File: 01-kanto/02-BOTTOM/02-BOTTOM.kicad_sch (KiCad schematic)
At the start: 0 parts

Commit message: 基板は2枚だけさ
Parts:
- added C2, C3, C4, C5, C6, C7, C9: 100n, symbol Device:C
- added C8: 4.7u, symbol Device:C
- added D2, D3, D4, D5: WS2812B, LED_SMD:LED_WS2812B_PLCC4_5.0x5.0mm_P3.2mm, symbol LED:WS2812B
- added R11, R12, R13, R14: 10k, symbol Device:R
- added SW6, SW7: SW_Push, symbol Switch:SW_Push
- added U2: STM32F103C8Tx, Package_QFP:LQFP-48_7x7mm_P0.5mm, symbol MCU_ST_STM32F1:STM32F103C8Tx
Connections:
- new net: D4.2 (DOUT), D5.4 (DIN)
- new net: D3.2 (DOUT), D4.4 (DIN)
- new net: D2.2 (DOUT), D3.4 (DIN)
- new net: R11.1, U2.20 (PB2)
- new net +3V3: C2.1, C3.1, C4.1, C5.1, C6.1, C7.1, C8.1, R13.2, R14.2, SW7.1, U2.1 (VBAT), U2.24 (VDD), U2.36 (VDD), U2.48 (VDD), U2.9 (VDDA)
- new net +5V: D2.1 (VDD), D3.1 (VDD), D4.1 (VDD), D5.1 (VDD)
- new net BOOT0: R12.1, SW7.2, U2.44 (BOOT0)
- new net GND: C2.2, C3.2, C4.2, C5.2, C6.2, C7.2, C8.2, C9.2, D2.3 (VSS), D3.3 (VSS), D4.3 (VSS), D5.3 (VSS), R11.2, R12.2, SW6.1, U2.23 (VSS), U2.35 (VSS), U2.47 (VSS), U2.8 (VSSA)
- new net LED: D2.4 (DIN)
- new net NRST: C9.1, SW6.2, U2.7 (NRST)
- new net SCL: R13.1, U2.42 (PB6)
- new net SDA: R14.1, U2.43 (PB7)
- new net UART1_RX: U2.31 (PA10)
- new net UART1_TX: U2.30 (PA9)
- no-connect marks 0 -> 6

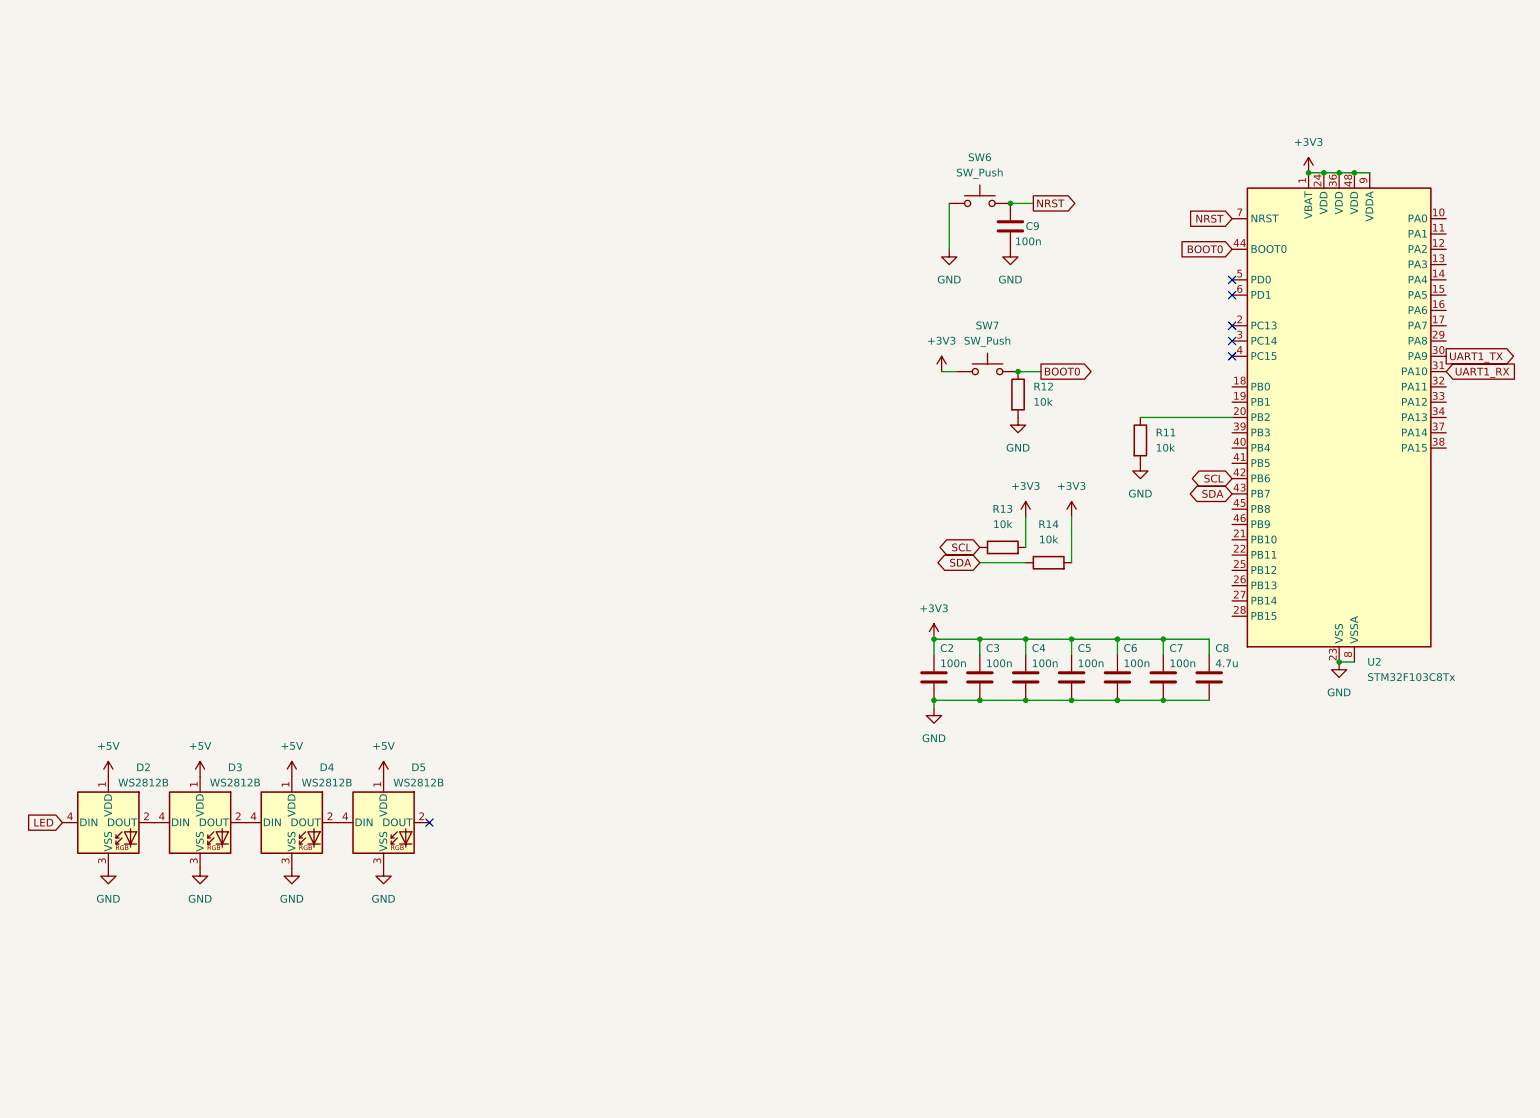
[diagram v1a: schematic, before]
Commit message: 02-BOTTOM schematic completed
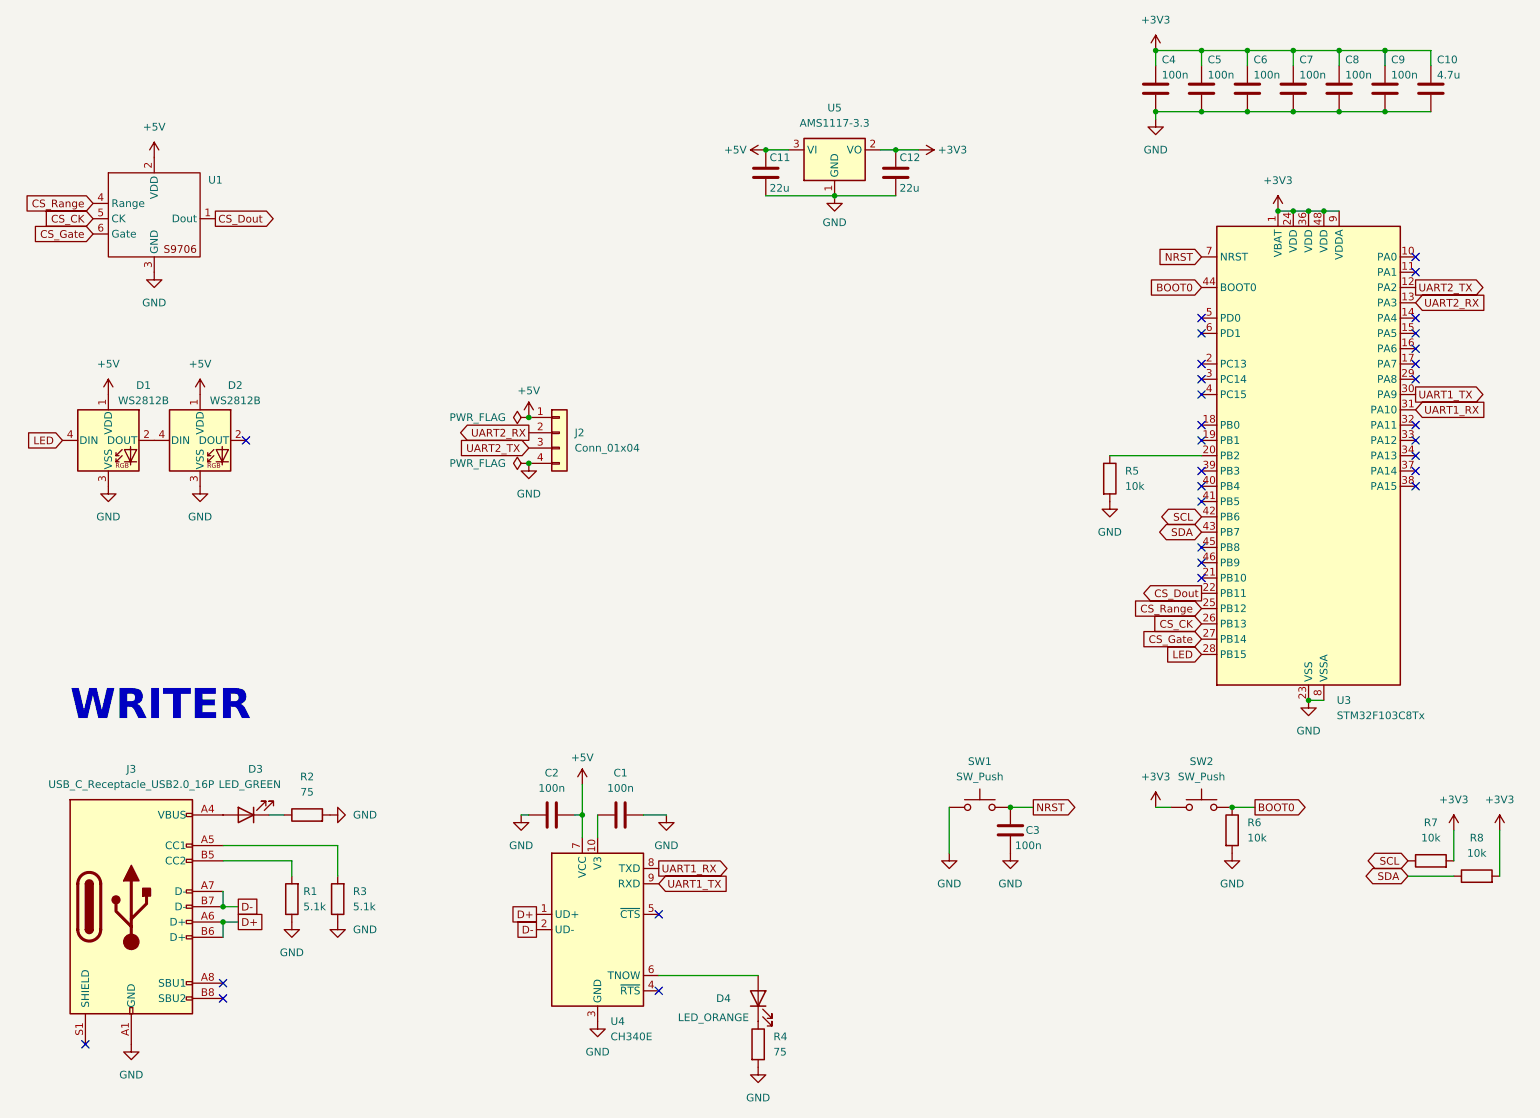
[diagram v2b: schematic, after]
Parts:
- removed D4, D5: WS2812B, LED_SMD:LED_WS2812B_PLCC4_5.0x5.0mm_P3.2mm, symbol LED:WS2812B
- added C1, C2: 100n, Capacitor_SMD:C_0402_1005Metric, symbol Device:C
- added C11, C12: 22u, Capacitor_SMD:C_0805_2012Metric, symbol Device:C
- added D3: LED_GREEN, LED_SMD:LED_1206_3216Metric, symbol Device:LED
- added D4: LED_ORANGE, LED_SMD:LED_1206_3216Metric, symbol Device:LED
- added J2: Conn_01x04, Connector_JST:JST_XH_B4B-XH-A_1x04_P2.50mm_Vertical, symbol Connector_Generic:Conn_01x04
- added J3: USB_C_Receptacle_USB2.0_16P, Connector_USB:USB_C_Receptacle_HCTL_HC-TYPE-C-16P-01A, symbol Connector:USB_C_Receptacle_USB2.0_16P
- added R1, R3: 5.1k, Resistor_SMD:R_0805_2012Metric, symbol Device:R
- added R2, R4: 75, Resistor_SMD:R_0805_2012Metric, symbol Device:R
- added U1: ~, Akizuki:S9706, symbol akizuki:S9706
- added U4: CH340E, Package_SO:MSOP-10_3x3mm_P0.5mm, symbol Interface_USB:CH340E
- added U5: AMS1117-3.3, Package_TO_SOT_SMD:SOT-223-3_TabPin2, symbol Regulator_Linear:AMS1117-3.3
- C10: renamed from C8; footprint (none) -> Capacitor_SMD:C_0603_1608Metric
- C3: renamed from C9; footprint (none) -> Capacitor_SMD:C_0402_1005Metric
- C4: renamed from C2; footprint (none) -> Capacitor_SMD:C_0402_1005Metric
- C5: renamed from C3; footprint (none) -> Capacitor_SMD:C_0402_1005Metric
- C6: renamed from C4; footprint (none) -> Capacitor_SMD:C_0402_1005Metric
- C7: renamed from C5; footprint (none) -> Capacitor_SMD:C_0402_1005Metric
- C8: renamed from C6; footprint (none) -> Capacitor_SMD:C_0402_1005Metric
- C9: renamed from C7; footprint (none) -> Capacitor_SMD:C_0402_1005Metric
- R5: renamed from R11; footprint (none) -> Resistor_SMD:R_0402_1005Metric
- R6: renamed from R12; footprint (none) -> Resistor_SMD:R_0402_1005Metric
- R7: renamed from R13; footprint (none) -> Resistor_SMD:R_0402_1005Metric
- R8: renamed from R14; footprint (none) -> Resistor_SMD:R_0402_1005Metric
- SW1: renamed from SW6; footprint (none) -> Button_Switch_THT:SW_PUSH_6mm
- SW2: renamed from SW7; footprint (none) -> Button_Switch_THT:SW_PUSH_6mm
- renumbered D2 to D1, D3 to D2, U2 to U3
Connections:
- net +3V3: now also C12.1, U5.2 (VO)
- net +5V: now also C11.1, C2.2, J2.1 (Pin_1), U1.2 (VDD), U4.7 (VCC), U5.3 (VI)
- net GND: now also C1.2, C11.2, C12.2, C2.1, J2.4 (Pin_4), J3.A1 (GND), J3.A12 (GND), J3.B1 (GND), J3.B12 (GND), R1.1, R2.2, R3.1, R4.2, U1.3 (GND), U4.3 (GND), U5.1 (GND)
- net LED: now also U3.28 (PB15)
- net UART1_RX: now also U4.8 (TXD)
- net UART1_TX: now also U4.9 (RXD)
- net UART2_TX: now reaches U3.12 (PA2)
- net UART2_TX: now also J2.3 (Pin_3)
- net UART2_RX: now reaches U3.13 (PA3)
- net UART2_RX: now also J2.2 (Pin_2)
- net CS_Dout: now reaches U3.22 (PB11)
- net CS_Dout: now also U1.1 (Dout)
- net CS_Range: now reaches U3.25 (PB12)
- net CS_Range: now also U1.4 (Range)
- net CS_CK: now reaches U3.26 (PB13)
- net CS_CK: now also U1.5 (CK)
- net CS_Gate: now reaches U3.27 (PB14)
- net CS_Gate: now also U1.6 (Gate)
- new net: C1.1, U4.10 (V3)
- new net: D3.1 (K), R2.1
- new net: D3.2 (A), J3.A4 (VBUS), J3.A9 (VBUS), J3.B4 (VBUS), J3.B9 (VBUS)
- new net: J3.B5 (CC2), R1.2
- new net: D4.1 (K), R4.1
- new net: D4.2 (A), U4.6 (TNOW)
- new net: J3.A5 (CC1), R3.2
- new net D+: J3.A6 (D+), J3.B6 (D+), U4.1 (UD+)
- new net D-: J3.A7 (D-), J3.B7 (D-), U4.2 (UD-)
- no-connect marks 6 -> 31
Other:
- note added: "WRITER"
- moved on the sheet: C10, C3, C4, C5, C6, C7, C8, C9, D1, D2, R5, R6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

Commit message: 02-BOTTOM placed parts
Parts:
- removed C9: 100n, Capacitor_SMD:C_0402_1005Metric, symbol Device:C
- J2: footprint Connector_JST:JST_XH_B4B-XH-A_1x04_P2.50mm_Vertical -> Connector_JST:JST_XH_S4B-XH-A_1x04_P2.50mm_Horizontal
- J3: footprint Connector_USB:USB_C_Receptacle_HCTL_HC-TYPE-C-16P-01A -> Connector_USB:USB_C_Receptacle_GCT_USB4105-xx-A_16P_TopMnt_Horizontal
- SW1, SW2: footprint Button_Switch_THT:SW_PUSH_6mm -> Akizuki:TVBP06_SW
- renumbered C10 to C9
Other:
- moved on the sheet: C9
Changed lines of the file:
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@@
 	)
 	(junction
-		(at 255.27 33.02)
-		(diameter 0)
-		(color 0 0 0 0)
-	)
-	(junction
 		(at 247.65 33.02)
 		(diameter 0)
@@
 	)
 	(junction
-		(at 255.27 22.86)
-		(diameter 0)
-		(color 0 0 0 0)
-	)
-	(junction
 		(at 113.03 91.44)
 		(diameter 0)
@@
 	(wire
 		(pts
-			(xy 262.89 22.86) (xy 262.89 25.4)
+			(xy 256.54 22.86) (xy 256.54 25.4)
 		)
 		(stroke
@@
 	(wire
 		(pts
-			(xy 247.65 33.02) (xy 255.27 33.02)
+			(xy 247.65 33.02) (xy 256.54 33.02)
 		)
 		(stroke
@@
 	(wire
 		(pts
-			(xy 255.27 33.02) (xy 262.89 33.02)
-		)
-		(stroke
-			(width 0)
-			(type default)
-		)
-	)
-	(wire
-		(pts
 			(xy 121.92 149.86) (xy 121.92 153.67)
 		)
@@
 	(wire
 		(pts
-			(xy 247.65 22.86) (xy 255.27 22.86)
+			(xy 247.65 22.86) (xy 256.54 22.86)
 		)
 		(stroke
@@
 	(wire
 		(pts
-			(xy 255.27 22.86) (xy 255.27 25.4)
-		)
-		(stroke
-			(width 0)
-			(type default)
-		)
-	)
-	(wire
-		(pts
 			(xy 111.76 149.86) (xy 113.03 149.86)
 		)
@@
 	(wire
 		(pts
-			(xy 255.27 22.86) (xy 262.89 22.86)
-		)
-		(stroke
-			(width 0)
-			(type default)
-		)
-	)
-	(wire
-		(pts
 			(xy 217.17 33.02) (xy 224.79 33.02)
 		)
@@
 	)
 	(symbol
-		(lib_id "Device:C")
-		(at 255.27 29.21 0)
-		(unit 1)
-		(exclude_from_sim no)
-		(in_bom yes)
-		(on_board yes)
-		(dnp no)
-		(property "Reference" "C9"
-			(at 256.286 24.384 0)
-			(effects
-				(font
-					(size 1.27 1.27)
-				)
-				(justify left)
-			)
-		)
-		(property "Value" "100n"
-			(at 256.286 26.924 0)
-			(effects
-				(font
-					(size 1.27 1.27)
-				)
-				(justify left)
-			)
-		)
-		(property "Footprint" "Capacitor_SMD:C_0402_1005Metric"
-			(at 256.2352 33.02 0)
-			(effects
-				(font
-					(size 1.27 1.27)
-				)
-				(hide yes)
-			)
-		)
-		(property "Datasheet" "~"
-			(at 255.27 29.21 0)
-			(effects
-				(font
-					(size 1.27 1.27)
-				)
-				(hide yes)
-			)
-		)
-		(property "Description" "Unpolarized capacitor"
-			(at 255.27 29.21 0)
-			(effects
-				(font
-					(size 1.27 1.27)
-				)
-				(hide yes)
-			)
-		)
-		(pin "2"
-		)
-		(pin "1"
-		)
-		(instances
-			(project "02-BOTTOM"
-				(path "/c169a242-17fe-4657-891f-5ce63e4a34fb"
-					(reference "C9")
-					(unit 1)
-				)
-			)
-		)
-	)
-	(symbol
 		(lib_name "LED_1")
 		(lib_id "Device:LED")
@@
 			)
 		)
-		(property "Footprint" "Connector_JST:JST_XH_B4B-XH-A_1x04_P2.50mm_Vertical"
+		(property "Footprint" "Connector_JST:JST_XH_S4B-XH-A_1x04_P2.50mm_Horizontal"
 			(at 118.11 86.36 0)
 			(effects
@@
 	(symbol
 		(lib_id "Device:C")
-		(at 262.89 29.21 0)
+		(at 256.54 29.21 0)
 		(unit 1)
 		(exclude_from_sim no)
@@
 		(on_board yes)
 		(dnp no)
-		(property "Reference" "C10"
-			(at 263.906 24.384 0)
+		(property "Reference" "C9"
+			(at 257.556 24.384 0)
 			(effects
 				(font
@@
 		)
 		(property "Value" "4.7u"
-			(at 263.906 26.924 0)
+			(at 257.556 26.924 0)
 			(effects
 				(font
@@
 		)
 		(property "Footprint" "Capacitor_SMD:C_0603_1608Metric"
-			(at 263.8552 33.02 0)
+			(at 257.5052 33.02 0)
 			(effects
 				(font
@@
 		)
 		(property "Datasheet" "~"
-			(at 262.89 29.21 0)
+			(at 256.54 29.21 0)
 			(effects
 				(font
@@
 		)
 		(property "Description" "Unpolarized capacitor"
-			(at 262.89 29.21 0)
+			(at 256.54 29.21 0)
 			(effects
 				(font
@@
 			(project "02-BOTTOM"
 				(path "/c169a242-17fe-4657-891f-5ce63e4a34fb"
-					(reference "C10")
+					(reference "C9")
 					(unit 1)
 				)
@@
 			)
 		)
-		(property "Footprint" "Button_Switch_THT:SW_PUSH_6mm"
+		(property "Footprint" "Akizuki:TVBP06_SW"
 			(at 224.79 143.51 0)
 			(effects
@@
 			)
 		)
-		(property "Footprint" "Button_Switch_THT:SW_PUSH_6mm"
+		(property "Footprint" "Akizuki:TVBP06_SW"
 			(at 187.96 143.51 0)
 			(effects
@@
 			)
 		)
-		(property "Footprint" "Connector_USB:USB_C_Receptacle_HCTL_HC-TYPE-C-16P-01A"
+		(property "Footprint" "Connector_USB:USB_C_Receptacle_GCT_USB4105-xx-A_16P_TopMnt_Horizontal"
 			(at 50.8 165.1 0)
 			(effects

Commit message: 02-BOTTOM PCBdesign completed
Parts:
- added D5: LED_GREEN, LED_SMD:LED_0805_2012Metric, symbol Device:LED
- added R9: 470, Resistor_SMD:R_0603_1608Metric, symbol Device:R
- C3, C4, C5, C6, C7, C8: LCSC (none) -> C1525
- C9: LCSC (none) -> C19666
- D3: footprint LED_SMD:LED_1206_3216Metric -> LED_SMD:LED_0805_2012Metric; LCSC C499475 -> C2297
- D4: value LED_ORANGE -> LED_YELLOW; LCSC C2764895 -> C2296
- J3: LCSC (none) -> C2765186
- R1, R3: footprint Resistor_SMD:R_0805_2012Metric -> Resistor_SMD:R_0402_1005Metric; LCSC C27834 -> C25905
- R2, R4: value 75 -> 470; footprint Resistor_SMD:R_0805_2012Metric -> Resistor_SMD:R_0603_1608Metric; LCSC C4275 -> C23179
- R5, R6, R7, R8: LCSC (none) -> C25744
- U3: LCSC (none) -> C8734
- U4: LCSC (none) -> C99652
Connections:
- net +3V3: now also U1.2 (VDD)
- net +5V: now also D5.2 (A); no longer U1.2 (VDD)
- net CS_CK: now also U3.40 (PB4); no longer U3.26 (PB13)
- net CS_Dout: now also U3.45 (PB8); no longer U3.22 (PB11)
- net CS_Gate: now also U3.39 (PB3); no longer U3.27 (PB14)
- net CS_Range: now also U3.41 (PB5); no longer U3.25 (PB12)
- net GND: now also R9.2
- net LED: now also U3.5 (PD0); no longer U3.28 (PB15)
- new net: D5.1 (K), R9.1
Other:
- moved on the sheet: R5

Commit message: 01-MAIN, 02-BOTTOM, 04-RPi totally completed
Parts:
- D4: footprint LED_SMD:LED_1206_3216Metric -> LED_SMD:LED_0805_2012Metric
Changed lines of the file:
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@@
 			)
 		)
-		(property "Footprint" "LED_SMD:LED_1206_3216Metric"
+		(property "Footprint" "LED_SMD:LED_0805_2012Metric"
 			(at 151.13 180.34 0)
 			(effects
